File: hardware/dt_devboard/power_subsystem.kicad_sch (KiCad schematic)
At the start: 1 part

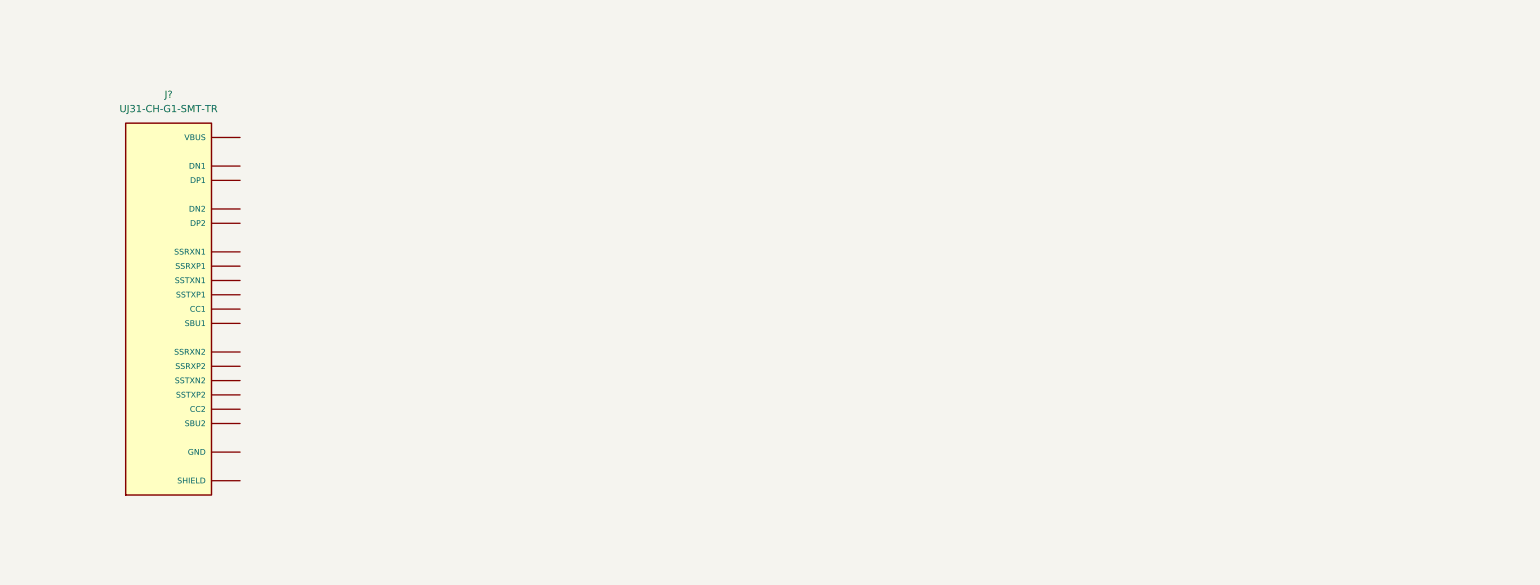
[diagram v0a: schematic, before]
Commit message: added library parts and schematic organization
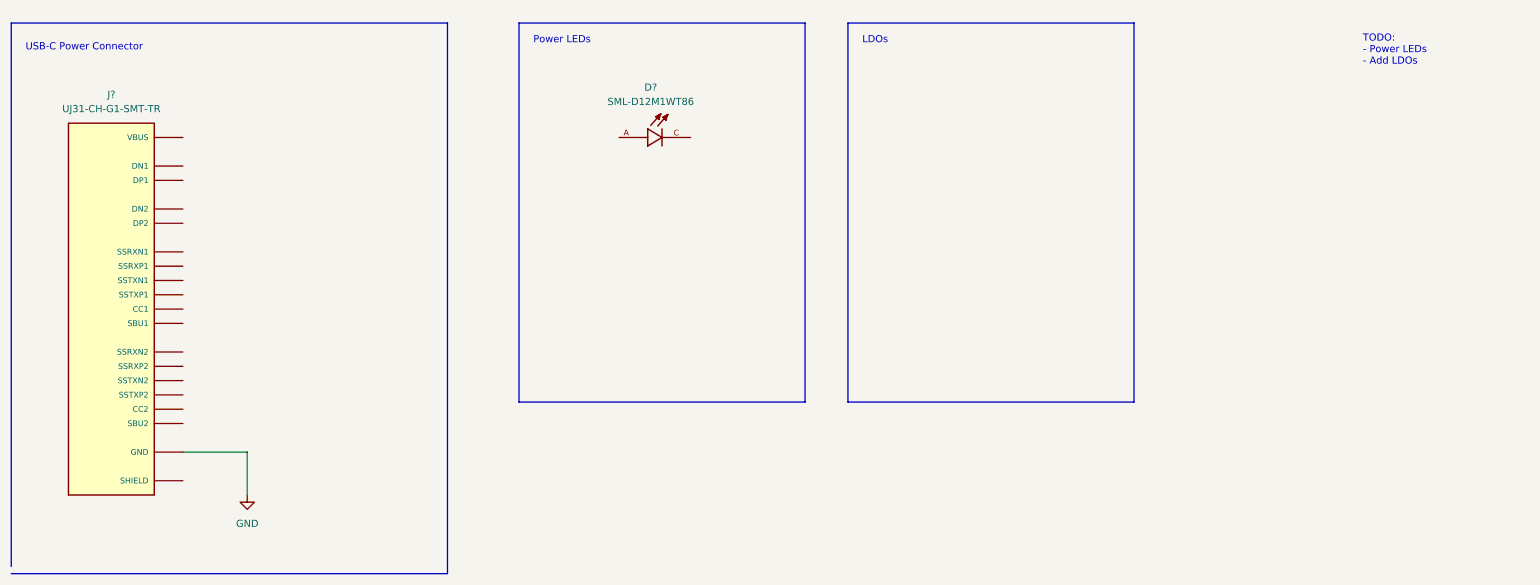
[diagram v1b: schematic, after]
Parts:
- added D?: SML-D12M1WT86, LED_SML-D12M1WT86, symbol SML-D12M1WT86:SML-D12M1WT86
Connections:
- net GND: now reaches J?.A1 (GND), J?.A12 (GND), J?.B1 (GND), J?.B12 (GND)
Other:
- note added: "LDOs"
- note added: "Power LEDs"
- note added: "TODO: - Power LEDs - Add LDOs"
- note added: "USB-C Power Connector"
- moved on the sheet: J?
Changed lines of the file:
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@@
 (kicad_sch (version 20211123) (generator eeschema)
   (paper "A4")
-  (symbol (lib_id "UJ31-CH-G1-SMT-TR:UJ31-CH-G1-SMT-TR") (at 46.99 66.04 0) (unit 1)
+  (polyline (pts (xy 19.05 111.76) (xy 19.05 15.24))
+    (stroke (width 0) (type default) (color 0 0 0 0))
+  )
+  (polyline (pts (xy 167.64 15.24) (xy 218.44 15.24))
+    (stroke (width 0) (type default) (color 0 0 0 0))
+  )
+  (polyline (pts (xy 109.22 15.24) (xy 109.22 82.55))
+    (stroke (width 0) (type default) (color 0 0 0 0))
+  )
+  (polyline (pts (xy 218.44 82.55) (xy 167.64 82.55))
+    (stroke (width 0) (type default) (color 0 0 0 0))
+  )
+  (polyline (pts (xy 218.44 15.24) (xy 218.44 82.55))
+    (stroke (width 0) (type default) (color 0 0 0 0))
+  )
+  (wire (pts (xy 49.53 91.44) (xy 60.96 91.44))
+    (stroke (width 0) (type default) (color 0 0 0 0))
+  )
+  (polyline (pts (xy 167.64 15.24) (xy 167.64 82.55))
+    (stroke (width 0) (type default) (color 0 0 0 0))
+  )
+  (polyline (pts (xy 19.05 113.03) (xy 96.52 113.03))
+    (stroke (width 0) (type default) (color 0 0 0 0))
+  )
+  (wire (pts (xy 60.96 91.44) (xy 60.96 99.06))
+    (stroke (width 0) (type default) (color 0 0 0 0))
+  )
+  (polyline (pts (xy 160.02 82.55) (xy 109.22 82.55))
+    (stroke (width 0) (type default) (color 0 0 0 0))
+  )
+  (polyline (pts (xy 160.02 15.24) (xy 160.02 82.55))
+    (stroke (width 0) (type default) (color 0 0 0 0))
+  )
+  (polyline (pts (xy 96.52 15.24) (xy 96.52 113.03))
+    (stroke (width 0) (type default) (color 0 0 0 0))
+  )
+  (polyline (pts (xy 109.22 15.24) (xy 160.02 15.24))
+    (stroke (width 0) (type default) (color 0 0 0 0))
+  )
+  (polyline (pts (xy 19.05 15.24) (xy 96.52 15.24))
+    (stroke (width 0) (type default) (color 0 0 0 0))
+  )
+  (text "LDOs\n" (at 170.18 19.05 0)
+    (effects (font (size 1.27 1.27)) (justify left bottom))
+  )
+  (text "TODO: \n- Power LEDs\n- Add LDOs \n" (at 259.08 22.86 0)
+    (effects (font (size 1.27 1.27)) (justify left bottom))
+  )
+  (text "Power LEDs\n" (at 111.76 19.05 0)
+    (effects (font (size 1.27 1.27)) (justify left bottom))
+  )
+  (text "USB-C Power Connector" (at 21.59 20.32 0)
+    (effects (font (size 1.27 1.27)) (justify left bottom))
+  )
+  (symbol (lib_id "UJ31-CH-G1-SMT-TR:UJ31-CH-G1-SMT-TR") (at 36.83 66.04 0) (unit 1)
     (in_bom yes) (on_board yes) (fields_autoplaced)
-    (property "Reference" "J?" (id 0) (at 46.99 27.94 0))
-    (property "Value" "UJ31-CH-G1-SMT-TR" (id 1) (at 46.99 30.48 0))
-    (property "Footprint" "CUI_UJ31-CH-G1-SMT-TR" (id 2) (at 46.99 66.04 0)
+    (property "Reference" "J?" (id 0) (at 36.83 27.94 0))
+    (property "Value" "UJ31-CH-G1-SMT-TR" (id 1) (at 36.83 30.48 0))
+    (property "Footprint" "CUI_UJ31-CH-G1-SMT-TR" (id 2) (at 36.83 66.04 0)
       (effects (font (size 1.27 1.27)) (justify left bottom) hide)
     )
-    (property "Datasheet" "" (id 3) (at 46.99 66.04 0)
+    (property "Datasheet" "" (id 3) (at 36.83 66.04 0)
       (effects (font (size 1.27 1.27)) (justify left bottom) hide)
     )
-    (property "MANUFACTURER" "CUI INC" (id 4) (at 46.99 66.04 0)
+    (property "MANUFACTURER" "CUI INC" (id 4) (at 36.83 66.04 0)
       (effects (font (size 1.27 1.27)) (justify left bottom) hide)
     )
-    (property "PART_REV" "1.01" (id 5) (at 46.99 66.04 0)
+    (property "PART_REV" "1.01" (id 5) (at 36.83 66.04 0)
       (effects (font (size 1.27 1.27)) (justify left bottom) hide)
     )
-    (property "STANDARD" "MANUFACTURER RECOMMENDATIONS" (id 6) (at 46.99 66.04 0)
+    (property "STANDARD" "MANUFACTURER RECOMMENDATIONS" (id 6) (at 36.83 66.04 0)
       (effects (font (size 1.27 1.27)) (justify left bottom) hide)
     )
@@
     (pin "SH6")
   )
+  (symbol (lib_id "power:GND") (at 60.96 99.06 0) (unit 1)
+    (in_bom yes) (on_board yes) (fields_autoplaced)
+    (property "Reference" "#PWR?" (id 0) (at 60.96 105.41 0)
+      (effects (font (size 1.27 1.27)) hide)
+    )
+    (property "Value" "GND" (id 1) (at 60.96 104.14 0))
+    (property "Footprint" "" (id 2) (at 60.96 99.06 0)
+      (effects (font (size 1.27 1.27)) hide)
+    )
+    (property "Datasheet" "" (id 3) (at 60.96 99.06 0)
+      (effects (font (size 1.27 1.27)) hide)
+    )
+    (pin "1")
+  )
+  (symbol (lib_id "SML-D12M1WT86:SML-D12M1WT86") (at 134.62 35.56 0) (unit 1)
+    (in_bom yes) (on_board yes) (fields_autoplaced)
+    (property "Reference" "D?" (id 0) (at 132.6134 26.67 0))
+    (property "Value" "SML-D12M1WT86" (id 1) (at 132.6134 29.21 0))
+    (property "Footprint" "LED_SML-D12M1WT86" (id 2) (at 134.62 35.56 0)
+      (effects (font (size 1.27 1.27)) (justify left bottom) hide)
+    )
+    (property "Datasheet" "" (id 3) (at 134.62 35.56 0)
+      (effects (font (size 1.27 1.27)) (justify left bottom) hide)
+    )
+    (property "MAXIMUM_PACKAGE_HEIGHT" "0.65 mm" (id 4) (at 134.62 35.56 0)
+      (effects (font (size 1.27 1.27)) (justify left bottom) hide)
+    )
+    (property "PARTREV" "007" (id 5) (at 134.62 35.56 0)
+      (effects (font (size 1.27 1.27)) (justify left bottom) hide)
+    )
+    (property "MANUFACTURER" "ROHM Semiconductor" (id 6) (at 134.62 35.56 0)
+      (effects (font (size 1.27 1.27)) (justify left bottom) hide)
+    )
+    (property "STANDARD" "Manufacturer Recommendation" (id 7) (at 134.62 35.56 0)
+      (effects (font (size 1.27 1.27)) (justify left bottom) hide)
+    )
+    (pin "A")
+    (pin "C")
+  )
   (sheet_instances
     (path "/" (page "1"))
   )
   (symbol_instances
+    (path "/5a889284-4c9f-49be-8f02-e43e18550914"
+      (reference "#PWR?") (unit 1) (value "GND") (footprint "")
+    )
+    (path "/60b6fd94-83fa-4737-bac1-4732bb229ea8"
+      (reference "D?") (unit 1) (value "SML-D12M1WT86") (footprint "LED_SML-D12M1WT86")
+    )
     (path "/38cad123-e6f8-46ac-bb65-7bf207c8a5a7"
       (reference "J?") (unit 1) (value "UJ31-CH-G1-SMT-TR") (footprint "CUI_UJ31-CH-G1-SMT-TR")

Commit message: added important USB nets
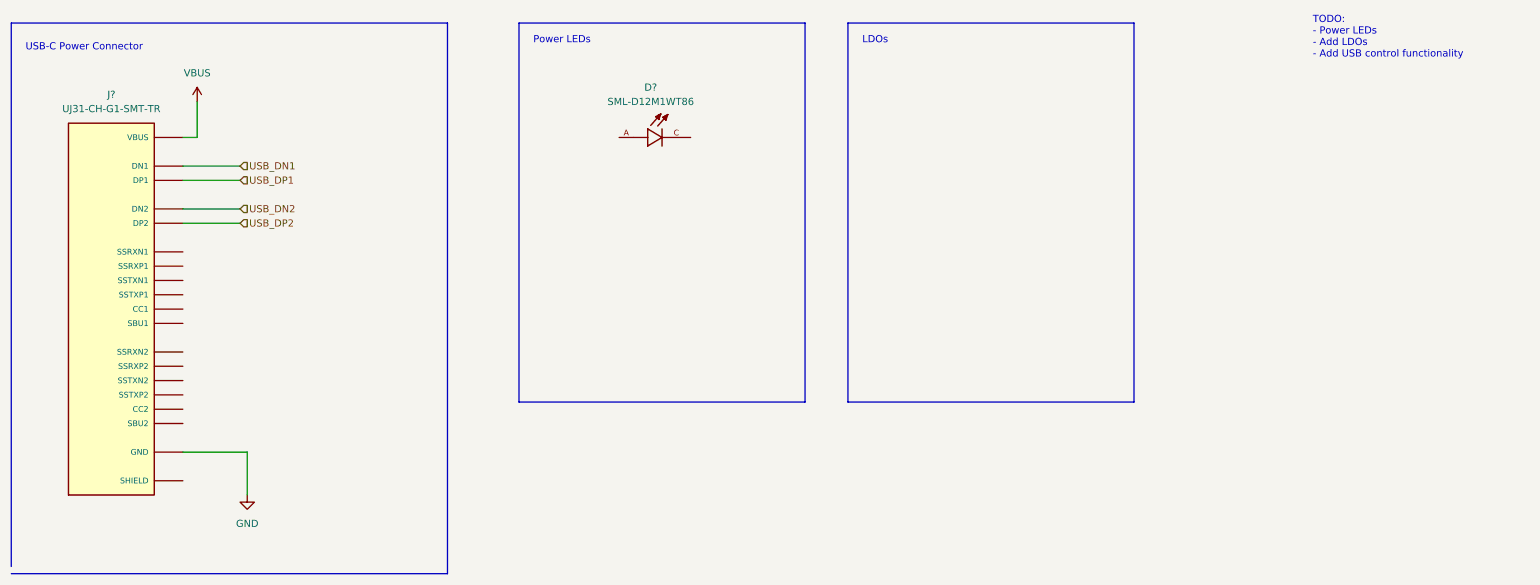
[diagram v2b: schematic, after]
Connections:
- net VBUS: now reaches J?.A4 (VBUS), J?.A9 (VBUS), J?.B4 (VBUS), J?.B9 (VBUS)
- net USB_DP1: now reaches J?.A6 (DP1)
- net USB_DN1: now reaches J?.A7 (DN1)
- net USB_DP2: now reaches J?.B6 (DP2)
- net USB_DN2: now reaches J?.B7 (DN2)
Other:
- note added: "TODO: - Power LEDs - Add LDOs - Add USB control functionality"
- note removed: "TODO: - Power LEDs - Add LDOs"
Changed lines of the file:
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@@
 (kicad_sch (version 20211123) (generator eeschema)
   (paper "A4")
+  (wire (pts (xy 49.53 35.56) (xy 52.07 35.56))
+    (stroke (width 0) (type default) (color 0 0 0 0))
+  )
+  (wire (pts (xy 49.53 48.26) (xy 59.69 48.26))
+    (stroke (width 0) (type default) (color 0 0 0 0))
+  )
   (polyline (pts (xy 19.05 111.76) (xy 19.05 15.24))
     (stroke (width 0) (type default) (color 0 0 0 0))
@@
     (stroke (width 0) (type default) (color 0 0 0 0))
   )
+  (wire (pts (xy 49.53 43.18) (xy 59.69 43.18))
+    (stroke (width 0) (type default) (color 0 0 0 0))
+  )
   (polyline (pts (xy 109.22 15.24) (xy 109.22 82.55))
+    (stroke (width 0) (type default) (color 0 0 0 0))
+  )
+  (wire (pts (xy 49.53 40.64) (xy 59.69 40.64))
     (stroke (width 0) (type default) (color 0 0 0 0))
   )
@@
     (stroke (width 0) (type default) (color 0 0 0 0))
   )
+  (wire (pts (xy 52.07 29.21) (xy 52.07 35.56))
+    (stroke (width 0) (type default) (color 0 0 0 0))
+  )
   (polyline (pts (xy 160.02 82.55) (xy 109.22 82.55))
     (stroke (width 0) (type default) (color 0 0 0 0))
   )
   (polyline (pts (xy 160.02 15.24) (xy 160.02 82.55))
+    (stroke (width 0) (type default) (color 0 0 0 0))
+  )
+  (wire (pts (xy 49.53 50.8) (xy 59.69 50.8))
     (stroke (width 0) (type default) (color 0 0 0 0))
   )
@@
     (effects (font (size 1.27 1.27)) (justify left bottom))
   )
-  (text "TODO: \n- Power LEDs\n- Add LDOs \n" (at 259.08 22.86 0)
+  (text "TODO: \n- Power LEDs\n- Add LDOs \n- Add USB control functionality\n"
+    (at 250.19 21.59 0)
     (effects (font (size 1.27 1.27)) (justify left bottom))
   )
@@
   (text "USB-C Power Connector" (at 21.59 20.32 0)
     (effects (font (size 1.27 1.27)) (justify left bottom))
+  )
+  (hierarchical_label "USB_DP2" (shape input) (at 59.69 50.8 0)
+    (effects (font (size 1.27 1.27)) (justify left))
+  )
+  (hierarchical_label "USB_DP1" (shape input) (at 59.69 43.18 0)
+    (effects (font (size 1.27 1.27)) (justify left))
+  )
+  (hierarchical_label "USB_DN1" (shape input) (at 59.69 40.64 0)
+    (effects (font (size 1.27 1.27)) (justify left))
+  )
+  (hierarchical_label "USB_DN2" (shape input) (at 59.69 48.26 0)
+    (effects (font (size 1.27 1.27)) (justify left))
+  )
+  (symbol (lib_id "power:VBUS") (at 52.07 29.21 0) (unit 1)
+    (in_bom yes) (on_board yes) (fields_autoplaced)
+    (property "Reference" "#PWR?" (id 0) (at 52.07 33.02 0)
+      (effects (font (size 1.27 1.27)) hide)
+    )
+    (property "Value" "VBUS" (id 1) (at 52.07 24.13 0))
+    (property "Footprint" "" (id 2) (at 52.07 29.21 0)
+      (effects (font (size 1.27 1.27)) hide)
+    )
+    (property "Datasheet" "" (id 3) (at 52.07 29.21 0)
+      (effects (font (size 1.27 1.27)) hide)
+    )
+    (pin "1")
   )
   (symbol (lib_id "UJ31-CH-G1-SMT-TR:UJ31-CH-G1-SMT-TR") (at 36.83 66.04 0) (unit 1)
@@
   )
   (symbol_instances
+    (path "/31cac15e-bcad-4ac1-ba6d-6a7d3365c9db"
+      (reference "#PWR?") (unit 1) (value "VBUS") (footprint "")
+    )
     (path "/5a889284-4c9f-49be-8f02-e43e18550914"
       (reference "#PWR?") (unit 1) (value "GND") (footprint "")
